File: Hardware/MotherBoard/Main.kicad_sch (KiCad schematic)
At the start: 16 parts, among them J9 Conn_02x02_Odd_Even, SW1 RESET_SW, U2 28C256, U3 WD65C22, U4 HM62256BLP, U5 WD65C02, X1 ACO-1MHz

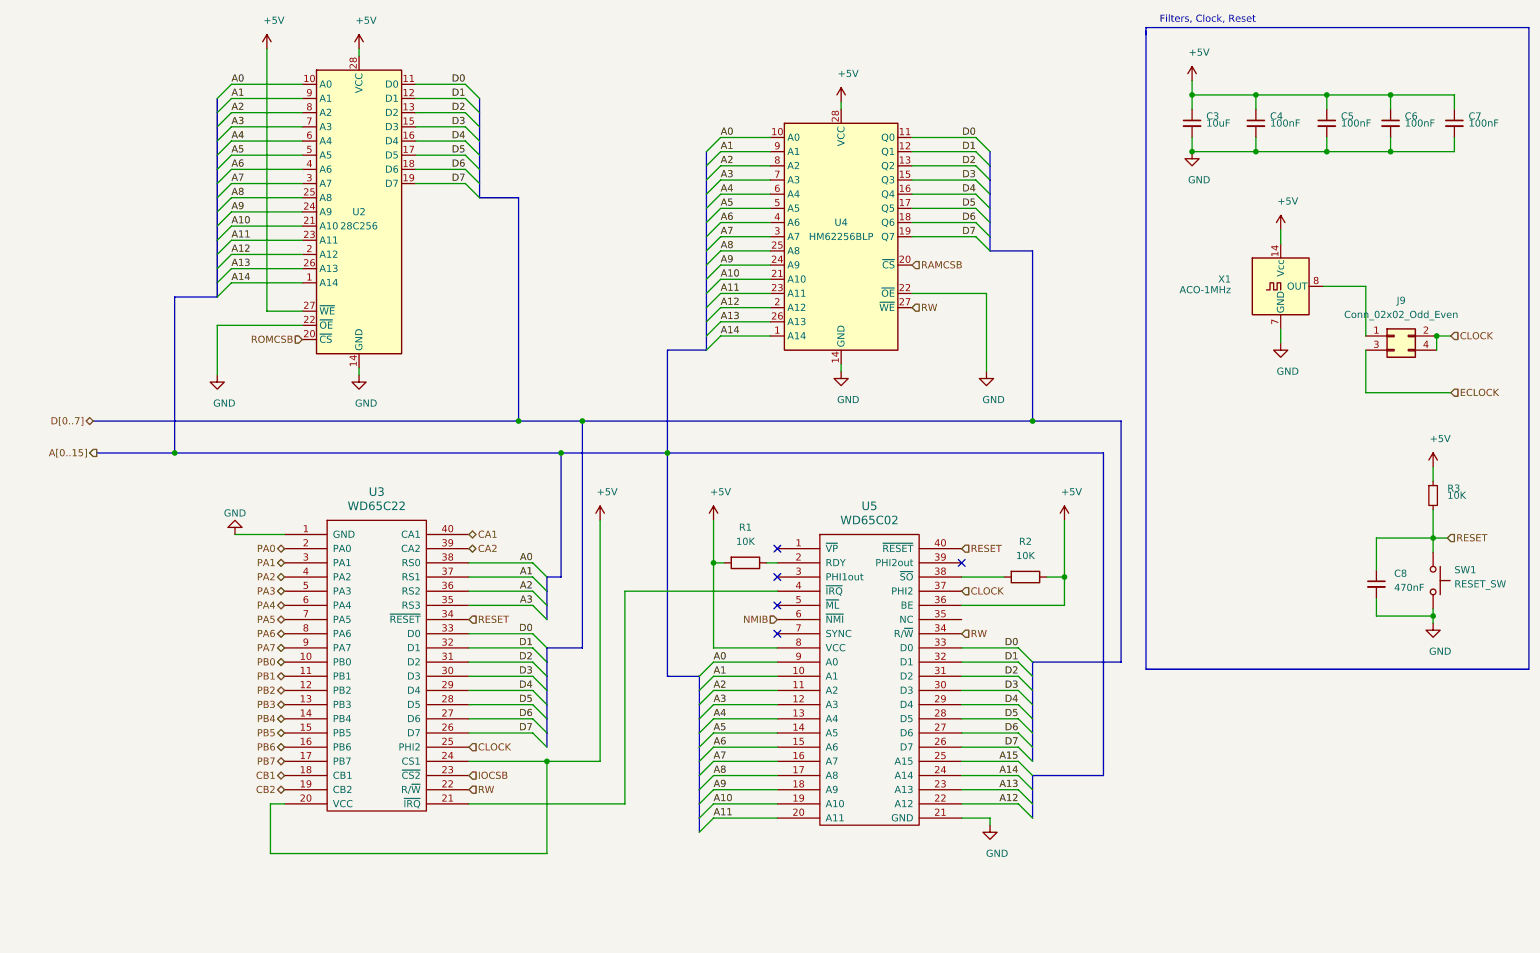
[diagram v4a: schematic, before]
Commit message: Implement APU and fix schematics
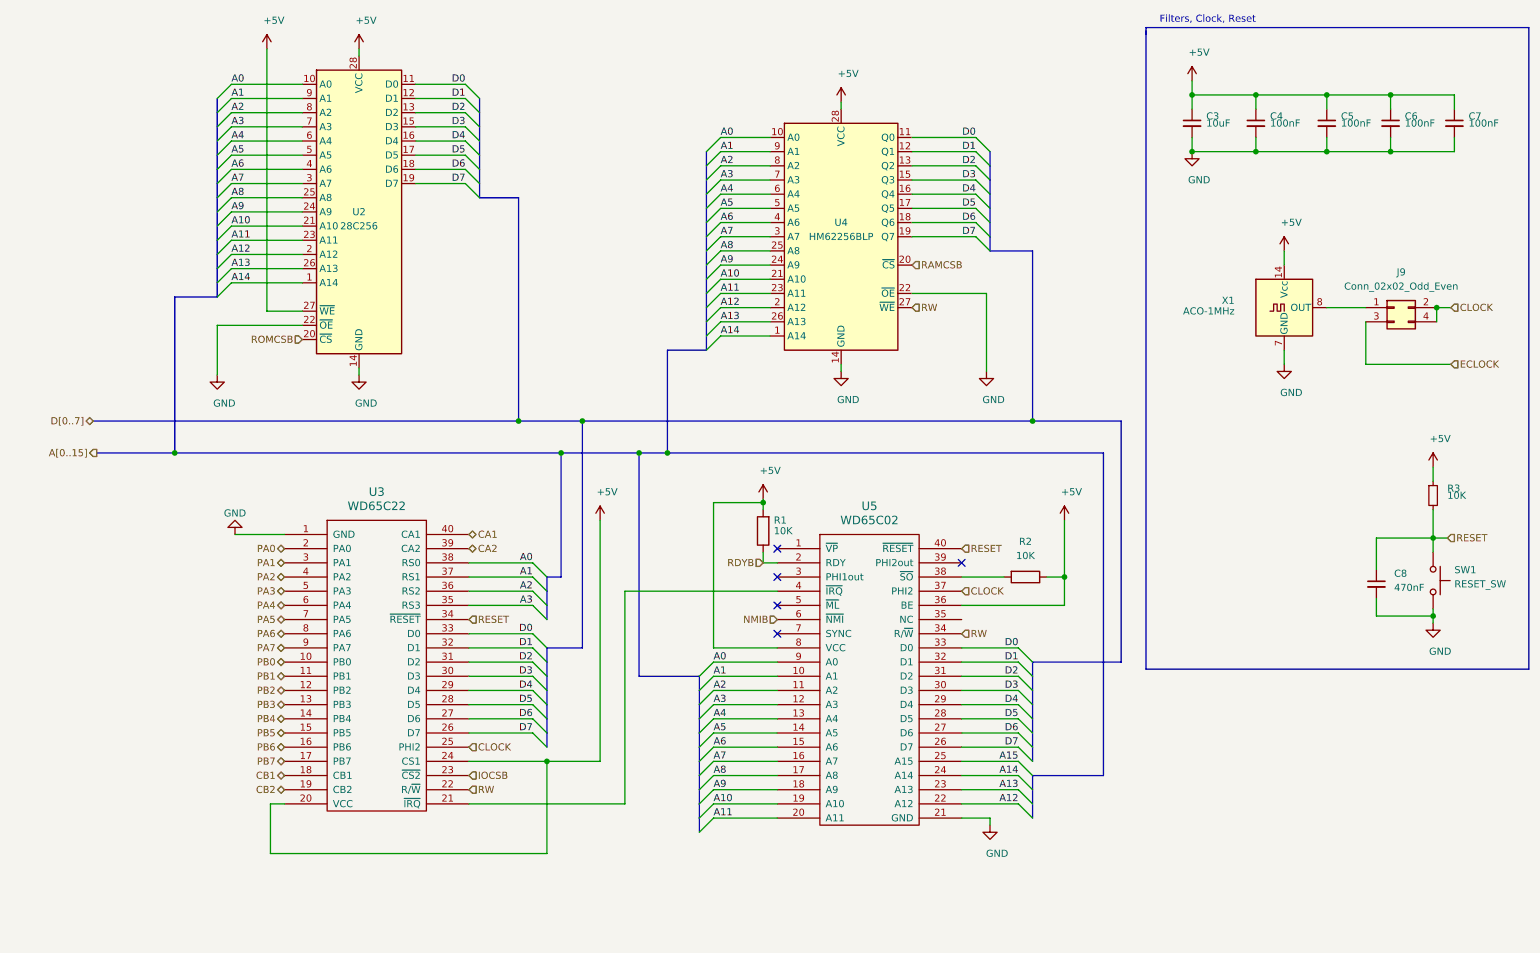
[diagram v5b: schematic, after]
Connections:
- net RDYB: now reaches R1.1, U5.2 (RDY)
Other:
- moved on the sheet: J9, R1, X1

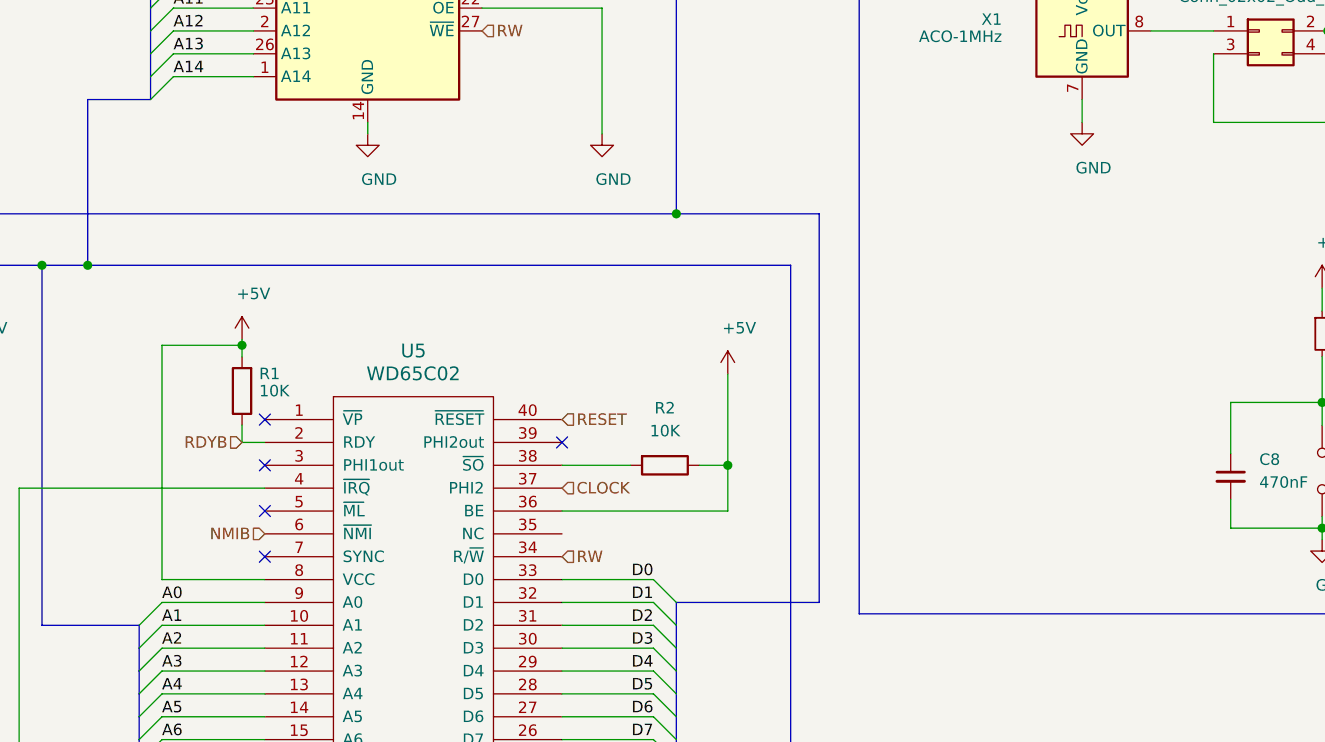
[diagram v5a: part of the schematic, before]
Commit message: Implement DMA and PCB ports
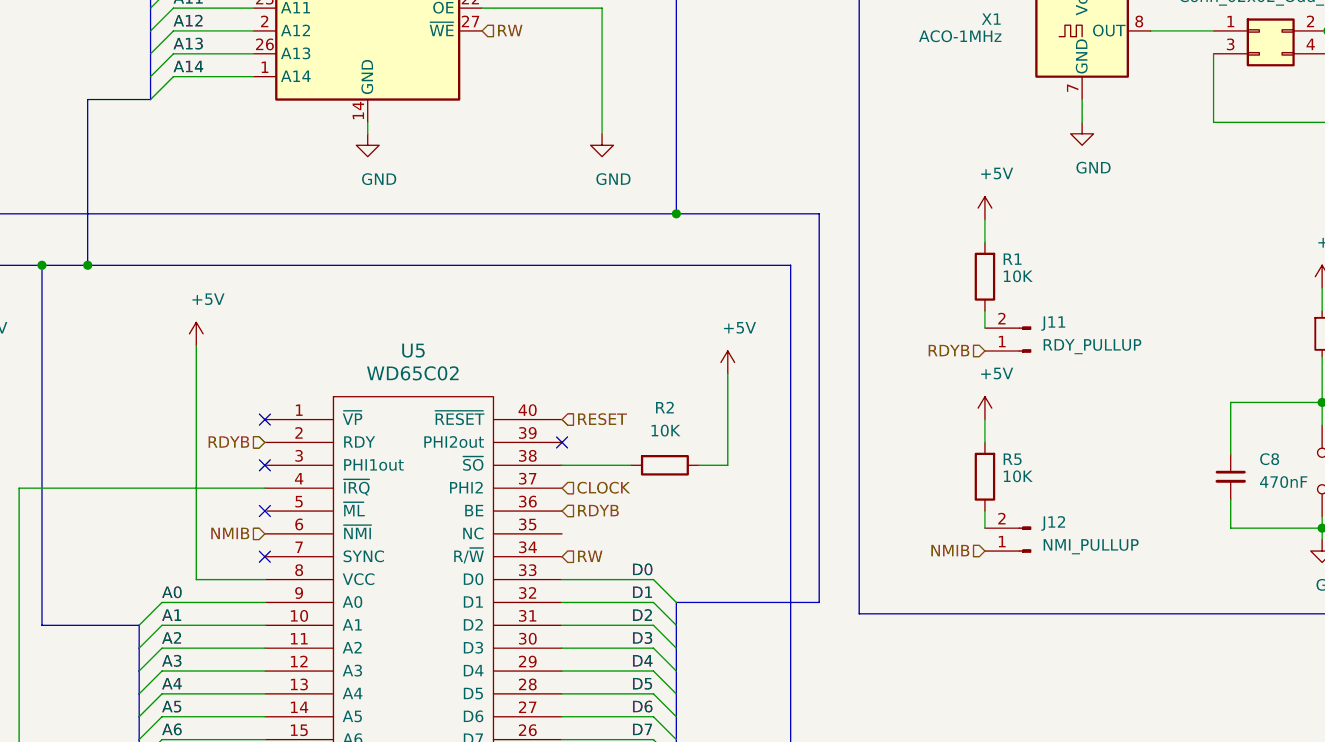
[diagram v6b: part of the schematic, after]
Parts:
- added J11: RDY_PULLUP, symbol Connector:Conn_01x02_Male
- added J12: NMI_PULLUP, symbol Connector:Conn_01x02_Male
- added R5: 10K, Resistor_THT:R_Axial_DIN0207_L6.3mm_D2.5mm_P10.16mm_Horizontal, symbol Device:R
- SW1: footprint Button_Switch_THT:SW_PUSH_6mm_H5mm -> Button_Switch_THT:SW_Tactile_SPST_Angled_PTS645Vx83-2LFS
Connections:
- net +5V: now also R5.2; no longer U5.36 (BE)
- net NMIB: now also J12.1 (Pin_1)
- net RDYB: now also U5.36 (BE), J11.1 (Pin_1); no longer R1.1
- new net: J11.2 (Pin_2), R1.1
- new net: J12.2 (Pin_2), R5.1
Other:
- moved on the sheet: R1

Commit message: Version 1.2
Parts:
- removed J11: RDY_PULLUP, symbol Connector:Conn_01x02_Male
- removed J12: NMI_PULLUP, symbol Connector:Conn_01x02_Male
- removed R1: 10K, Resistor_THT:R_Axial_DIN0207_L6.3mm_D2.5mm_P10.16mm_Horizontal, symbol Device:R
- C8: footprint Capacitor_THT:C_Disc_D5.0mm_W2.5mm_P2.50mm -> Capacitor_THT:C_Disc_D5.0mm_W2.5mm_P5.00mm
- U2: value 28C256 -> AT28C256
- U4: value HM62256BLP -> AS6C62256
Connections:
- net +5V: no longer R5.2
- net RDYB: now also R5.2; no longer U5.2 (RDY)
- net at R5.1: now also U5.2 (RDY)
- net IRQ1B: now reaches U3.21 (~IRQ)
- net IRQ1B: no longer U5.4 (~IRQ)
- new net IRQB: U5.4 (~IRQ)
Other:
- moved on the sheet: R2, U3, U4, U5

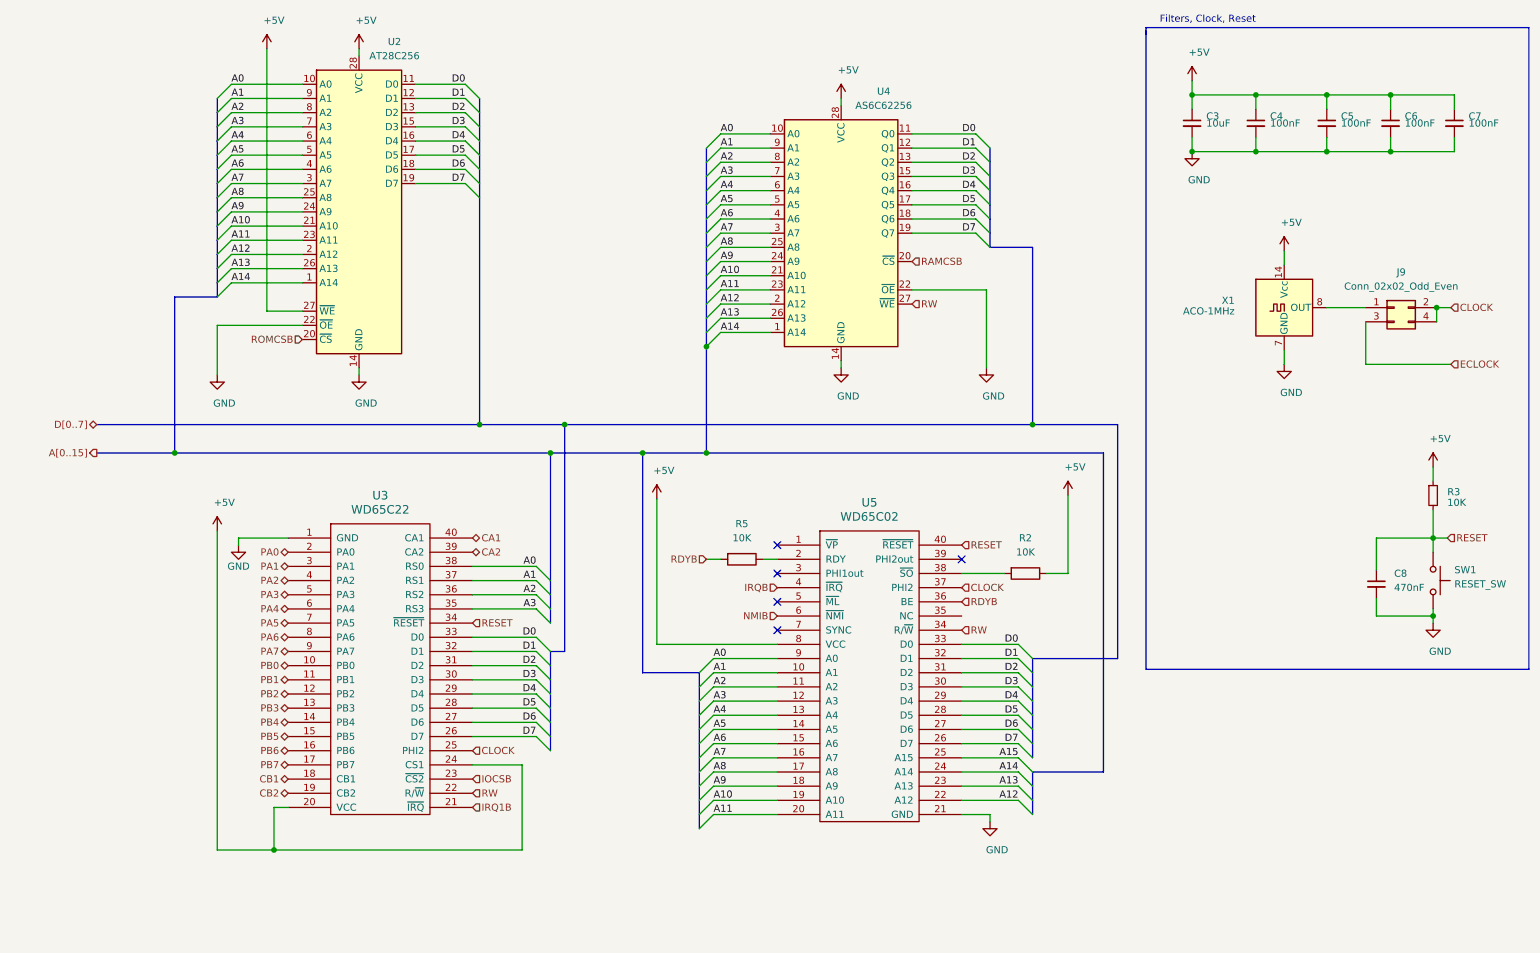
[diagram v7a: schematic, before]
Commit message: New PLD logic, VGA, DMA ...
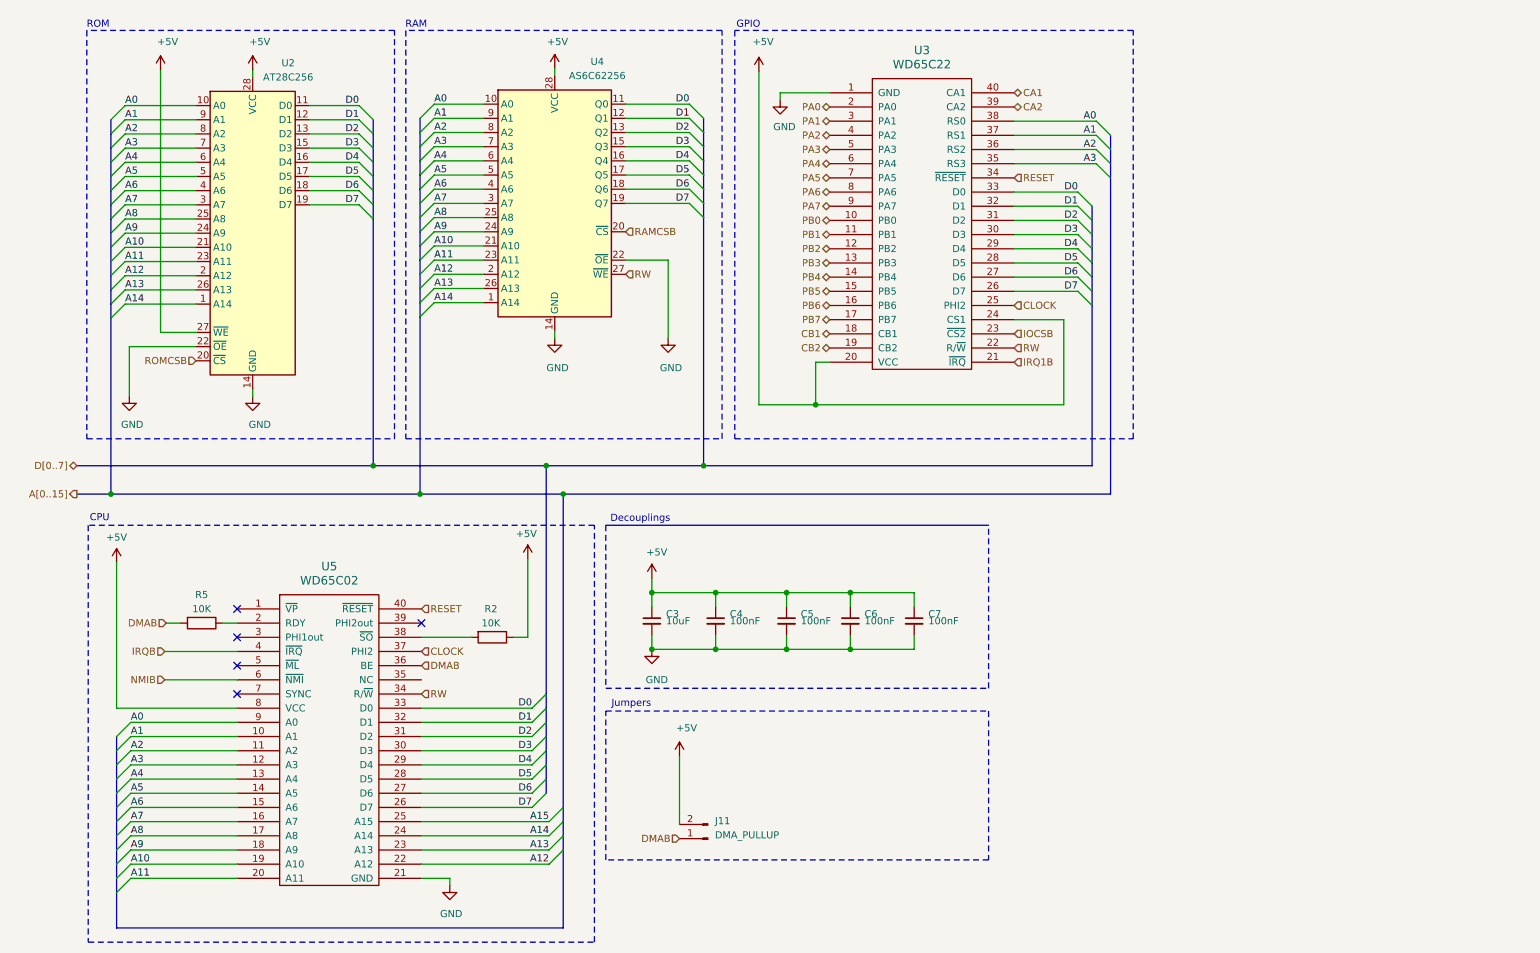
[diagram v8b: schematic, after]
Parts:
- removed C8: 470nF, Capacitor_THT:C_Disc_D5.0mm_W2.5mm_P5.00mm, symbol Device:C_Small
- removed J9: Conn_02x02_Odd_Even, Connector_PinHeader_2.54mm:PinHeader_2x02_P2.54mm_Vertical, symbol Connector_Generic:Conn_02x02_Odd_Even
- removed R3: 10K, Resistor_THT:R_Axial_DIN0207_L6.3mm_D2.5mm_P10.16mm_Horizontal, symbol Device:R_Small
- removed SW1: RESET_SW, Button_Switch_THT:SW_Tactile_SPST_Angled_PTS645Vx83-2LFS, symbol Switch:SW_Push
- removed X1: ACO-1MHz, Oscillator:Oscillator_DIP-14, symbol Oscillator:ACO-xxxMHz
- added J11: DMA_PULLUP, Connector_PinHeader_2.54mm:PinHeader_1x02_P2.54mm_Vertical, symbol Connector:Conn_01x02_Male
- U2: footprint Package_DIP:DIP-28_W15.24mm -> Socket:DIP_Socket-28_W11.9_W12.7_W15.24_W17.78_W18.5_3M_228-1277-00-0602J
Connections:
- net +5V: now also J11.2 (Pin_2)
- net RDYB renamed DMAB
- net DMAB: now also J11.1 (Pin_1)
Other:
- note added: "CPU"
- note added: "Decouplings"
- note added: "GPIO"
- note added: "Jumpers"
- note added: "RAM"
- note added: "ROM"
- note removed: "Filters, Clock, Reset"
- moved on the sheet: C3, C4, C5, C6, C7, R2, R5, U2, U3, U4, U5
